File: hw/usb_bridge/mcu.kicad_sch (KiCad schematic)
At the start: 10 parts, among them J3 SWD, J4 BOOT, U7 STM32G0B1CBT, Y2 HCI XC53G2-8.000-F12NJHP

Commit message: Add license
Signed-off-by: Mateusz Pająk <22417805+Tai-Min@users.noreply.github.com>
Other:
- note added: "This documentation describes Open Hardware and is licensed under the CERN OHL v. 1.2. You may redistribute and modify this documentation under the terms of the CERN OHL v.1.2.(http://ohwr.org/cernohl). This documentation is distributed WITHOUT ANY EXPRESS OR IMPLIED WARRANTY, INCLUDING OF MERCHANTABILITY, SATISFACTORY QUALITY AND FITNESS FOR A PARTICULAR PURPOSE. Please see the CERN OHL v.1.2 for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"
- title: (none) -> USB <-> CAN/RS485 Bridge
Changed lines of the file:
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@@
 	(generator_version "9.0")
 	(paper "A4")
+	(title_block
+		(title "USB <-> CAN/RS485 Bridge")
+		(date "2025-11-24")
+		(rev "1.0")
+	)
 	(text "VREF/VDD"
 		(exclude_from_sim no)
@@
 		(effects
 			(font
+				(size 1.27 1.27)
+			)
+		)
+	)
+	(text "This documentation describes Open Hardware and is licensed under the CERN OHL v. 1.2.\nYou may redistribute and modify this documentation under the terms of the \nCERN OHL v.1.2.(http://ohwr.org/cernohl). This documentation is distributed \nWITHOUT ANY EXPRESS OR IMPLIED WARRANTY, INCLUDING OF MERCHANTABILITY,\nSATISFACTORY QUALITY AND FITNESS FOR A PARTICULAR PURPOSE.\nPlease see the CERN OHL v.1.2 for applicable conditions"
+		(exclude_from_sim no)
+		(at 231.394 174.244 0)
+		(effects
+			(font

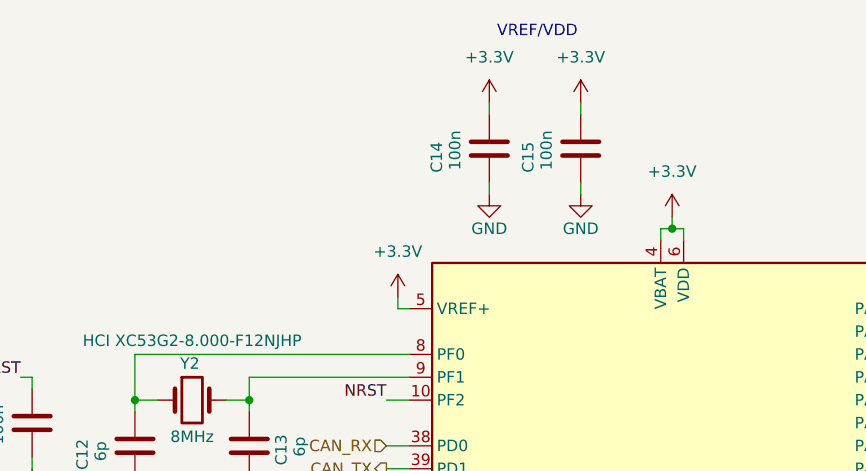
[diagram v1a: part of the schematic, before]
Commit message: Add jumpers and test points, add QR code
Signed-off-by: Mateusz Pająk <22417805+Tai-Min@users.noreply.github.com>
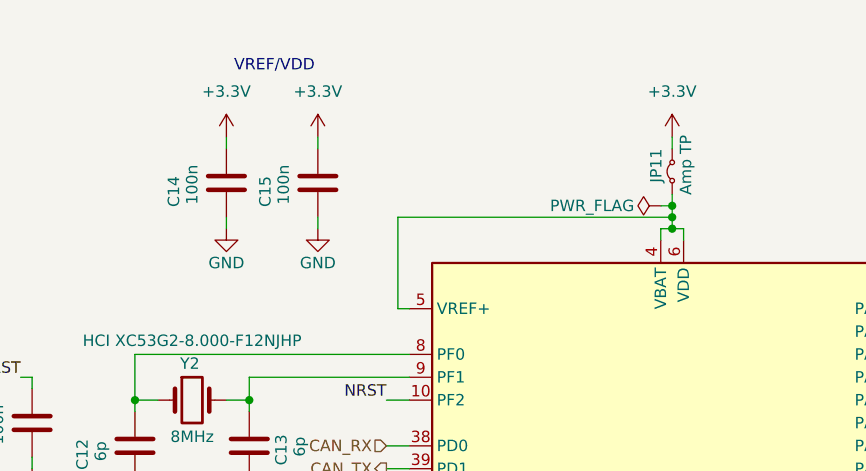
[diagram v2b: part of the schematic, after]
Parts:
- added JP11: Amp TP, Jumper:SolderJumper-2_P1.3mm_Bridged_Pad1.0x1.5mm, symbol Jumper:Jumper_2_Small_Bridged
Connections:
- net +3.3V: now also JP11.2 (B); no longer U7.4 (VBAT), U7.5 (VREF+), U7.6 (VDD)
- new net: JP11.1 (A), U7.4 (VBAT), U7.5 (VREF+), U7.6 (VDD)
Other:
- moved on the sheet: C14, C15

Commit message: Change versioning
Signed-off-by: Mateusz Pająk <22417805+Tai-Min@users.noreply.github.com>
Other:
- title: USB <-> CAN/RS485 Bridge -> ${TITLE}
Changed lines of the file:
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@@
 	(paper "A4")
 	(title_block
-		(title "USB <-> CAN/RS485 Bridge")
+		(title "${TITLE}")
 		(date "2025-11-24")
-		(rev "1.0")
+		(rev "${REVISION}")
 	)
 	(text "VREF/VDD"

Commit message: Update LCSC BOM
Signed-off-by: Mateusz Pająk <22417805+Tai-Min@users.noreply.github.com>
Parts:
- C11, C14, C15: LCSC https://www.lcsc.com/product-detail/C66501.html -> (none); LCSC Link (none) -> https://www.lcsc.com/product-detail/C66501.html; LCSC Part # (none) -> C66501
- C12, C13: LCSC https://www.lcsc.com/product-detail/C170142.html -> (none); LCSC Link (none) -> https://www.lcsc.com/product-detail/C170142.html; LCSC Part # (none) -> C170142
- J3: LCSC https://www.lcsc.com/product-detail/C7494874.html -> (none); LCSC Link (none) -> https://www.lcsc.com/product-detail/C7494874.html; LCSC Part # (none) -> C7494874
- J4: LCSC https://www.lcsc.com/product-detail/C7494857.html -> (none); LCSC Link (none) -> https://www.lcsc.com/product-detail/C7494857.html; LCSC Part # (none) -> C7494857
- R16: LCSC https://www.lcsc.com/product-detail/C98220.html -> (none); LCSC Link (none) -> https://www.lcsc.com/product-detail/C98220.html; LCSC Part # (none) -> C98220
- U7: LCSC https://www.lcsc.com/product-detail/C2847904.html?s_z=n_STM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 -> (none); LCSC Link (none) -> https://www.lcsc.com/product-detail/C2847904.html?s_z=n_STM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; LCSC Part # (none) -> C2847904
- Y2: LCSC https://www.lcsc.com/product-detail/C2842269.html -> (none); LCSC Link (none) -> https://www.lcsc.com/product-detail/C2842269.html; LCSC Part # (none) -> C2842269
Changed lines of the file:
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@@
-			)
-		)
-		(property "LCSC" "https://www.lcsc.com/product-detail/C2842269.html"
-			(at 109.22 71.12 0)
-			(effects
-				(font
-					(size 1.27 1.27)
-				)
-				(hide yes)
 			)
 		)
@@
 			)
 		)
+		(property "LCSC Link" "https://www.lcsc.com/product-detail/C2842269.html"
+			(at 109.22 71.12 0)
+			(effects
+				(font
+					(size 1.27 1.27)
+				)
+				(hide yes)
+			)
+		)
+		(property "LCSC Part #" "C2842269"
+			(at 109.22 71.12 0)
+			(effects
+				(font
+					(size 1.27 1.27)
+				)
+				(hide yes)
+			)
+		)
 		(pin "1"
 		)
@@
 			)
 		)
-		(property "LCSC" "https://www.lcsc.com/product-detail/C66501.html"
+		(property "LCSC Link" "https://www.lcsc.com/product-detail/C66501.html"
 			(at 91.44 73.66 90)
 			(effects
@@
 			)
 		)
-		(property "Field5" ""
+		(property "LCSC Part #" "C66501"
 			(at 91.44 73.66 90)
 			(effects
@@
 			)
 		)
-		(property "LCSC" "https://www.lcsc.com/product-detail/C170142.html"
+		(property "LCSC Link" "https://www.lcsc.com/product-detail/C170142.html"
 			(at 102.87 76.2 90)
 			(effects
@@
 			)
 		)
-		(property "Field5" ""
+		(property "LCSC Part #" "C170142"
 			(at 102.87 76.2 90)
 			(effects
@@
 			)
 		)
-		(property "LCSC" "https://www.lcsc.com/product-detail/C7494874.html"
+		(property "LCSC Link" "https://www.lcsc.com/product-detail/C7494874.html"
 			(at 100.33 106.68 0)
 			(effects
@@
 			)
 		)
-		(property "Field5" ""
+		(property "LCSC Part #" "C7494874"
 			(at 100.33 106.68 0)
 			(effects
@@
 			)
 		)
+		(property "LCSC Part #" ""
+			(at 162.56 45.72 0)
+			(effects
+				(font
+					(size 1.27 1.27)
+				)
+				(hide yes)
+			)
+		)
 		(pin "1"
 		)
@@
 			)
 		)
-		(property "LCSC" "https://www.lcsc.com/product-detail/C2847904.html?s_z=n_STM32G0B1CBT"
+		(property "LCSC Link" "https://www.lcsc.com/product-detail/C2847904.html?s_z=n_STM32G0B1CBT"
 			(at 161.29 101.6 0)
 			(effects
@@
 			)
 		)
-		(property "Field5" ""
+		(property "LCSC Part #" "C2847904"
 			(at 161.29 101.6 0)
 			(effects
@@
 			)
 		)
-		(property "LCSC" "https://www.lcsc.com/product-detail/C66501.html"
+		(property "LCSC Link" "https://www.lcsc.com/product-detail/C66501.html"
 			(at 123.19 46.99 90)
 			(effects
@@
 			)
 		)
-		(property "Field5" ""
+		(property "LCSC Part #" "C66501"
 			(at 123.19 46.99 90)
 			(effects
@@
 			)
 		)
-		(property "LCSC" "https://www.lcsc.com/product-detail/C98220.html"
+		(property "LCSC Link" "https://www.lcsc.com/product-detail/C98220.html"
 			(at 99.06 134.62 0)
 			(effects
@@
 			)
 		)
-		(property "Field5" ""
+		(property "LCSC Part #" "C98220"
 			(at 99.06 134.62 0)
 			(effects
@@
 			)
 		)
-		(property "LCSC" "https://www.lcsc.com/product-detail/C7494857.html"
+		(property "LCSC Link" "https://www.lcsc.com/product-detail/C7494857.html"
 			(at 105.41 127 0)
 			(effects
@@
 			)
 		)
-		(property "Field5" ""
+		(property "LCSC Part #" "C7494857"
 			(at 105.41 127 0)
 			(effects
@@
 			)
 		)
-		(property "LCSC" "https://www.lcsc.com/product-detail/C170142.html"
+		(property "LCSC Link" "https://www.lcsc.com/product-detail/C170142.html"
 			(at 115.57 76.2 90)
 			(effects
@@
 			)
 		)
-		(property "Field5" ""
+		(property "LCSC Part #" "C170142"
 			(at 115.57 76.2 90)
 			(effects
@@
 			)
 		)
-		(property "LCSC" "https://www.lcsc.com/product-detail/C66501.html"
+		(property "LCSC Link" "https://www.lcsc.com/product-detail/C66501.html"
 			(at 113.03 46.99 90)
 			(effects
@@
 			)
 		)
-		(property "Field5" ""
+		(property "LCSC Part #" "C66501"
 			(at 113.03 46.99 90)
 			(effects

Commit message: Update datasheets
Signed-off-by: Mateusz Pająk <22417805+Tai-Min@users.noreply.github.com>
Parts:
- C11, C14, C15: LCSC Link https://www.lcsc.com/product-detail/C66501.html -> (none)
- C12, C13: LCSC Link https://www.lcsc.com/product-detail/C170142.html -> (none)
- J3: LCSC Link https://www.lcsc.com/product-detail/C7494874.html -> (none)
- J4: LCSC Link https://www.lcsc.com/product-detail/C7494857.html -> (none)
- R16: LCSC Link https://www.lcsc.com/product-detail/C98220.html -> (none)
- U7: LCSC Link https://www.lcsc.com/product-detail/C2847904.html?s_z=n_STM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 -> (none)
- Y2: Freq 8MHz -> (none); LCSC Link https://www.lcsc.com/product-detail/C2842269.html -> (none)
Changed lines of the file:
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@@
 			)
 		)
-		(property "Description" "Two pin crystal"
-			(at 109.22 71.12 0)
-			(effects
-				(font
-					(size 1.27 1.27)
-				)
-				(hide yes)
-			)
-		)
-		(property "Freq" "8MHz"
+		(property "Description" "8MHz"
 			(at 109.22 75.184 0)
 			(effects
@@
 					(size 1.27 1.27)
 				)
-			)
-		)
-		(property "LCSC Link" "https://www.lcsc.com/product-detail/C2842269.html"
-			(at 109.22 71.12 0)
-			(effects
-				(font
-					(size 1.27 1.27)
-				)
-				(hide yes)
 			)
 		)
@@
 			)
 		)
-		(property "LCSC Link" "https://www.lcsc.com/product-detail/C66501.html"
-			(at 91.44 73.66 90)
-			(effects
-				(font
-					(size 1.27 1.27)
-				)
-				(hide yes)
-			)
-		)
 		(property "LCSC Part #" "C66501"
 			(at 91.44 73.66 90)
@@
 		(property "Description" "Unpolarized capacitor"
 			(at 102.87 76.2 0)
-			(effects
-				(font
-					(size 1.27 1.27)
-				)
-				(hide yes)
-			)
-		)
-		(property "LCSC Link" "https://www.lcsc.com/product-detail/C170142.html"
-			(at 102.87 76.2 90)
 			(effects
 				(font
@@
 			)
 		)
-		(property "LCSC Link" "https://www.lcsc.com/product-detail/C7494874.html"
-			(at 100.33 106.68 0)
-			(effects
-				(font
-					(size 1.27 1.27)
-				)
-				(hide yes)
-			)
-		)
 		(property "LCSC Part #" "C7494874"
 			(at 100.33 106.68 0)
@@
 			)
 		)
-		(property "Datasheet" "\\datasheets\\stm32g0b1cb-2.pdf"
+		(property "Datasheet" "\\datasheets\\STM32G0B1CBT.pdf"
 			(at 161.29 101.6 0)
 			(effects
@@
 		)
 		(property "Description" "STMicroelectronics Arm Cortex-M0+ MCU, 128KB flash, 144KB RAM, 64 MHz, 1.7-3.6V, 44 GPIO, LQFP48"
-			(at 161.29 101.6 0)
-			(effects
-				(font
-					(size 1.27 1.27)
-				)
-				(hide yes)
-			)
-		)
-		(property "LCSC Link" "https://www.lcsc.com/product-detail/C2847904.html?s_z=n_STM32G0B1CBT"
 			(at 161.29 101.6 0)
 			(effects
@@
 			)
 		)
-		(property "LCSC Link" "https://www.lcsc.com/product-detail/C66501.html"
-			(at 123.19 46.99 90)
-			(effects
-				(font
-					(size 1.27 1.27)
-				)
-				(hide yes)
-			)
-		)
 		(property "LCSC Part #" "C66501"
 			(at 123.19 46.99 90)
@@
 		)
 		(property "Description" "Resistor"
-			(at 99.06 134.62 0)
-			(effects
-				(font
-					(size 1.27 1.27)
-				)
-				(hide yes)
-			)
-		)
-		(property "LCSC Link" "https://www.lcsc.com/product-detail/C98220.html"
 			(at 99.06 134.62 0)
 			(effects
@@
 			)
 		)
-		(property "LCSC Link" "https://www.lcsc.com/product-detail/C7494857.html"
-			(at 105.41 127 0)
-			(effects
-				(font
-					(size 1.27 1.27)
-				)
-				(hide yes)
-			)
-		)
 		(property "LCSC Part #" "C7494857"
 			(at 105.41 127 0)
@@
 		(property "Description" "Unpolarized capacitor"
 			(at 115.57 76.2 0)
-			(effects
-				(font
-					(size 1.27 1.27)
-				)
-				(hide yes)
-			)
-		)
-		(property "LCSC Link" "https://www.lcsc.com/product-detail/C170142.html"
-			(at 115.57 76.2 90)
 			(effects
 				(font
@@
 			(effects
 				(font
-					(size 1.27 1.27)
-				)
-				(hide yes)
-			)
-		)
-		(property "LCSC Link" "https://www.lcsc.com/product-detail/C66501.html"
-			(at 113.03 46.99 90)
-			(effects
-				(font

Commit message: Cleanup
Signed-off-by: Mateusz Pająk <22417805+Tai-Min@users.noreply.github.com>
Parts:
- removed JP11: Amp TP, Jumper:SolderJumper-2_P1.3mm_Bridged_Pad1.0x1.5mm, symbol Jumper:Jumper_2_Small_Bridged
- renumbered C14 to C13, C13 to C14, R16 to R15
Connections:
- net +3.3V: now also U7.4 (VBAT), U7.5 (VREF+), U7.6 (VDD)
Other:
- note removed: "This documentation describes Open Hardware and is licensed under the CERN OHL v. 1.2. You may redistribute and modify this documentation under the terms of the CERN OHL v.1.2.(http://ohwr.org/cernohl). This documentation is distributed WITHOUT ANY EXPRESS OR IMPLIED WARRANTY, INCLUDING OF MERCHANTABILITY, SATISFACTORY QUALITY AND FITNESS FOR A PARTICULAR PURPOSE. Please see the CERN OHL v.1.2 for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"
